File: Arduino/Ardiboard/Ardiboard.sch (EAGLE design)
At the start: 10 parts, among them IC1 ATMEGA168-20P, J1 1X5, U1 ARDUINOR3-BPLACE

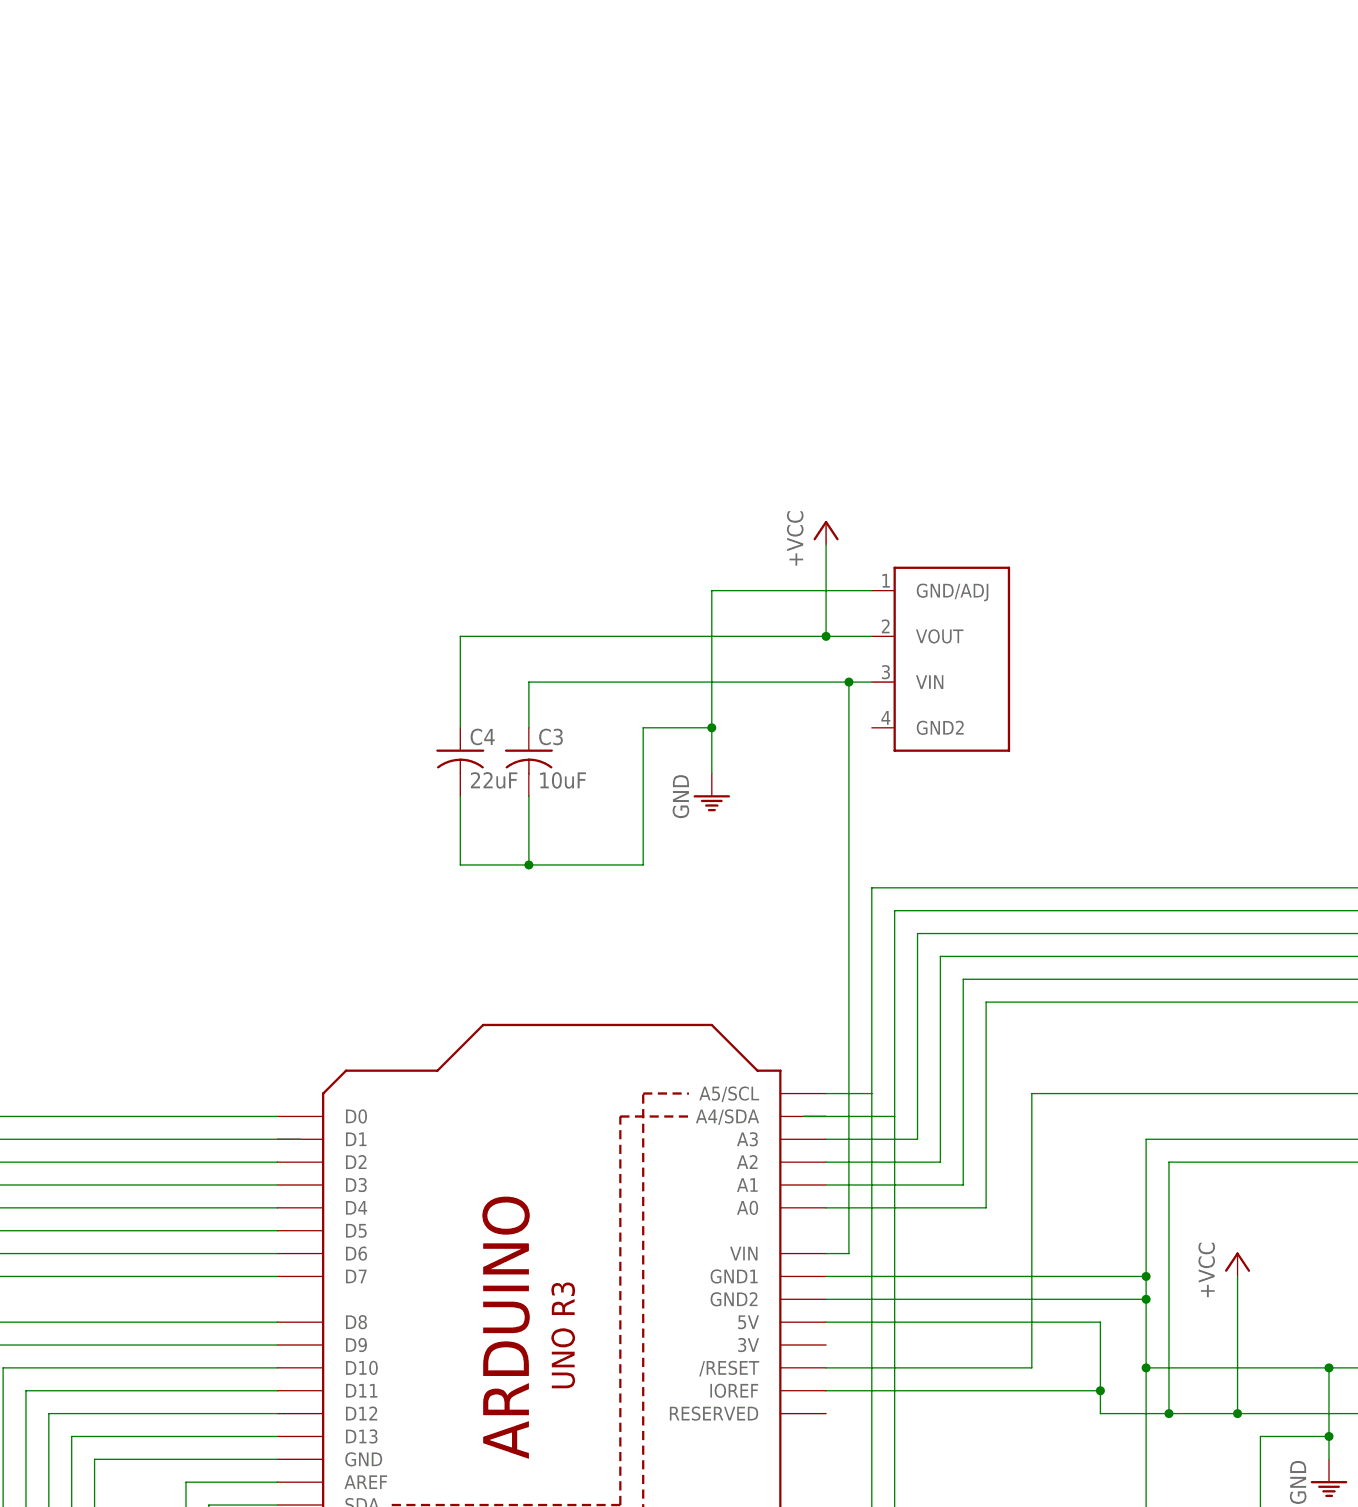
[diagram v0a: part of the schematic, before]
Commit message: added 3.3V regulator
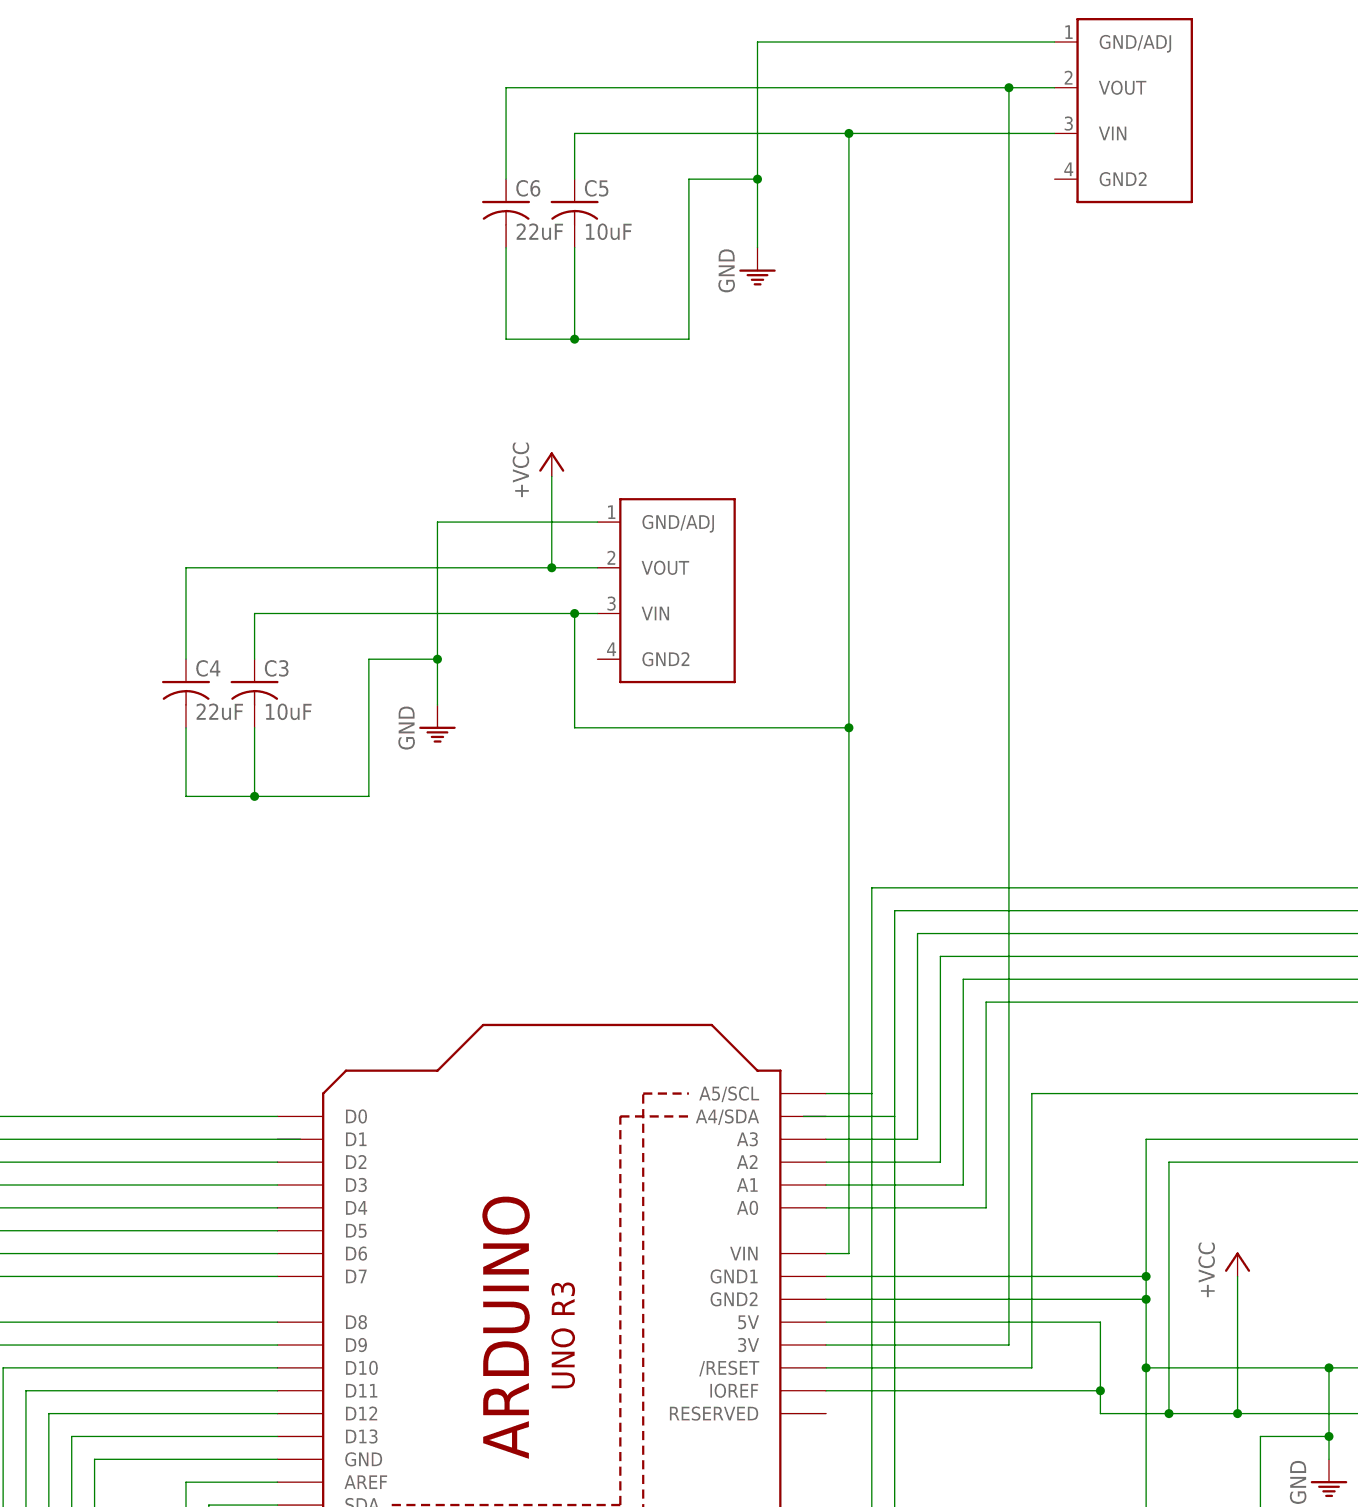
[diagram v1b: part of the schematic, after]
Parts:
- removed U$1: AZ1086-XX, voltage:AZ1086-XX
- added C5: 10uF, rcl:C-US025-030X050
- added C6: 22uF, rcl:C-US025-030X050
- added Q2: AZ1086H-5.0, voltage:AZ1086-XX
- added Q3: AZ1086H-3.3, voltage:AZ1086-XX
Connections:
- new net N$25: C3.1, C5.1, Q2.VIN, Q3.VIN, U1.VIN
- net +5V: now also Q2.VOUT; no longer U$1.VOUT
- net N$24: now also C6.1, Q3.VOUT, U1.3V; no longer C3.1, U$1.VIN, U1.VIN
- net PE: now also C5.2, C6.2, Q2.GND/ADJ, Q3.GND/ADJ; no longer U$1.GND/ADJ
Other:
- moved on the sheet: C3, C4
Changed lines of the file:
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@@
 <?xml version="1.0" encoding="utf-8"?>
 <!DOCTYPE eagle SYSTEM "eagle.dtd">
-<eagle version="6.5.0">
+<eagle version="6.6.0">
 <drawing>
 <settings>
@@
 <part name="C2" library="rcl" deviceset="C-US" device="025-025X050"/>
 <part name="P+3" library="power" deviceset="+VCC" device=""/>
-<part name="U$1" library="voltage" deviceset="AZ1086-XX" device=""/>
+<part name="Q2" library="voltage" deviceset="AZ1086-XX" device="" value="AZ1086H-5.0"/>
 <part name="GND3" library="power" deviceset="GND" device=""/>
 <part name="P+4" library="power" deviceset="+VCC" device=""/>
@@
 <part name="P+5" library="power" deviceset="+VCC" device=""/>
 <part name="GND4" library="power" deviceset="GND" device=""/>
+<part name="Q3" library="voltage" deviceset="AZ1086-XX" device="" value="AZ1086H-3.3"/>
+<part name="GND5" library="power" deviceset="GND" device=""/>
+<part name="C5" library="rcl" deviceset="C-US" device="025-030X050" value="10uF"/>
+<part name="C6" library="rcl" deviceset="C-US" device="025-030X050" value="22uF"/>
 </parts>
 <sheets>
@@
 <instance part="C2" gate="G$1" x="116.84" y="33.02"/>
 <instance part="P+3" gate="1" x="-22.86" y="33.02"/>
-<instance part="U$1" gate="G$1" x="66.04" y="132.08"/>
-<instance part="GND3" gate="M" x="40.64" y="114.3"/>
-<instance part="P+4" gate="1" x="53.34" y="144.78"/>
-<instance part="C3" gate="G$1" x="20.32" y="119.38"/>
-<instance part="C4" gate="G$1" x="12.7" y="119.38"/>
+<instance part="Q2" gate="G$1" x="35.56" y="139.7"/>
+<instance part="GND3" gate="M" x="10.16" y="121.92"/>
+<instance part="P+4" gate="1" x="22.86" y="152.4"/>
+<instance part="C3" gate="G$1" x="-10.16" y="127"/>
+<instance part="C4" gate="G$1" x="-17.78" y="127"/>
 <instance part="JP1" gate="G$1" x="248.92" y="38.1"/>
 <instance part="P+5" gate="1" x="259.08" y="60.96"/>
 <instance part="GND4" gate="M" x="259.08" y="17.78"/>
+<instance part="Q3" gate="G$1" x="86.36" y="193.04"/>
+<instance part="GND5" gate="M" x="45.72" y="172.72"/>
+<instance part="C5" gate="G$1" x="25.4" y="180.34"/>
+<instance part="C6" gate="G$1" x="17.78" y="180.34"/>
 </instances>
 <busses>
@@
 </segment>
 <segment>
-<pinref part="U$1" gate="G$1" pin="GND/ADJ"/>
-<wire x1="58.42" y1="137.16" x2="40.64" y2="137.16" width="0.1524" layer="91"/>
-<wire x1="40.64" y1="137.16" x2="40.64" y2="121.92" width="0.1524" layer="91"/>
-<wire x1="40.64" y1="121.92" x2="40.64" y2="116.84" width="0.1524" layer="91"/>
+<pinref part="Q2" gate="G$1" pin="GND/ADJ"/>
+<wire x1="27.94" y1="144.78" x2="10.16" y2="144.78" width="0.1524" layer="91"/>
+<wire x1="10.16" y1="144.78" x2="10.16" y2="129.54" width="0.1524" layer="91"/>
+<wire x1="10.16" y1="129.54" x2="10.16" y2="124.46" width="0.1524" layer="91"/>
 <pinref part="GND3" gate="M" pin="PE"/>
-<wire x1="40.64" y1="121.92" x2="33.02" y2="121.92" width="0.1524" layer="91"/>
-<wire x1="33.02" y1="121.92" x2="33.02" y2="106.68" width="0.1524" layer="91"/>
-<wire x1="33.02" y1="106.68" x2="20.32" y2="106.68" width="0.1524" layer="91"/>
-<wire x1="20.32" y1="106.68" x2="20.32" y2="114.3" width="0.1524" layer="91"/>
-<wire x1="20.32" y1="106.68" x2="12.7" y2="106.68" width="0.1524" layer="91"/>
-<wire x1="12.7" y1="106.68" x2="12.7" y2="114.3" width="0.1524" layer="91"/>
-<junction x="20.32" y="106.68"/>
-<junction x="40.64" y="121.92"/>
+<wire x1="10.16" y1="129.54" x2="2.54" y2="129.54" width="0.1524" layer="91"/>
+<wire x1="2.54" y1="129.54" x2="2.54" y2="114.3" width="0.1524" layer="91"/>
+<wire x1="2.54" y1="114.3" x2="-10.16" y2="114.3" width="0.1524" layer="91"/>
+<wire x1="-10.16" y1="114.3" x2="-10.16" y2="121.92" width="0.1524" layer="91"/>
+<wire x1="-10.16" y1="114.3" x2="-17.78" y2="114.3" width="0.1524" layer="91"/>
+<wire x1="-17.78" y1="114.3" x2="-17.78" y2="121.92" width="0.1524" layer="91"/>
+<junction x="-10.16" y="114.3"/>
+<junction x="10.16" y="129.54"/>
 <pinref part="C3" gate="G$1" pin="2"/>
 <pinref part="C4" gate="G$1" pin="2"/>
@@
 <wire x1="259.08" y1="35.56" x2="259.08" y2="20.32" width="0.1524" layer="91"/>
 <pinref part="GND4" gate="M" pin="PE"/>
+</segment>
+<segment>
+<pinref part="Q3" gate="G$1" pin="GND/ADJ"/>
+<wire x1="78.74" y1="198.12" x2="45.72" y2="198.12" width="0.1524" layer="91"/>
+<wire x1="45.72" y1="198.12" x2="45.72" y2="182.88" width="0.1524" layer="91"/>
+<wire x1="45.72" y1="182.88" x2="45.72" y2="175.26" width="0.1524" layer="91"/>
+<pinref part="GND5" gate="M" pin="PE"/>
+<wire x1="45.72" y1="182.88" x2="38.1" y2="182.88" width="0.1524" layer="91"/>
+<wire x1="38.1" y1="182.88" x2="38.1" y2="165.1" width="0.1524" layer="91"/>
+<wire x1="38.1" y1="165.1" x2="25.4" y2="165.1" width="0.1524" layer="91"/>
+<wire x1="25.4" y1="165.1" x2="25.4" y2="175.26" width="0.1524" layer="91"/>
+<wire x1="25.4" y1="165.1" x2="17.78" y2="165.1" width="0.1524" layer="91"/>
+<wire x1="17.78" y1="165.1" x2="17.78" y2="175.26" width="0.1524" layer="91"/>
+<junction x="25.4" y="165.1"/>
+<junction x="45.72" y="182.88"/>
+<pinref part="C5" gate="G$1" pin="2"/>
+<pinref part="C6" gate="G$1" pin="2"/>
 </segment>
 </net>
@@
 <segment>
 <pinref part="P+4" gate="1" pin="+5V"/>
-<wire x1="53.34" y1="142.24" x2="53.34" y2="132.08" width="0.1524" layer="91"/>
-<pinref part="U$1" gate="G$1" pin="VOUT"/>
-<wire x1="53.34" y1="132.08" x2="58.42" y2="132.08" width="0.1524" layer="91"/>
-<wire x1="53.34" y1="132.08" x2="12.7" y2="132.08" width="0.1524" layer="91"/>
-<wire x1="12.7" y1="132.08" x2="12.7" y2="121.92" width="0.1524" layer="91"/>
-<junction x="53.34" y="132.08"/>
+<wire x1="22.86" y1="149.86" x2="22.86" y2="139.7" width="0.1524" layer="91"/>
+<pinref part="Q2" gate="G$1" pin="VOUT"/>
+<wire x1="22.86" y1="139.7" x2="27.94" y2="139.7" width="0.1524" layer="91"/>
+<wire x1="22.86" y1="139.7" x2="-17.78" y2="139.7" width="0.1524" layer="91"/>
+<wire x1="-17.78" y1="139.7" x2="-17.78" y2="129.54" width="0.1524" layer="91"/>
+<junction x="22.86" y="139.7"/>
 <pinref part="C4" gate="G$1" pin="1"/>
 </segment>
@@
 </segment>
 </net>
-<net name="N$24" class="0">
+<net name="N$25" class="0">
 <segment>
 <pinref part="U1" gate="G$1" pin="VIN"/>
 <wire x1="53.34" y1="63.5" x2="55.88" y2="63.5" width="0.1524" layer="91"/>
-<wire x1="55.88" y1="63.5" x2="55.88" y2="127" width="0.1524" layer="91"/>
-<pinref part="U$1" gate="G$1" pin="VIN"/>
-<wire x1="55.88" y1="127" x2="58.42" y2="127" width="0.1524" layer="91"/>
-<wire x1="55.88" y1="127" x2="20.32" y2="127" width="0.1524" layer="91"/>
-<junction x="55.88" y="127"/>
+<wire x1="55.88" y1="63.5" x2="55.88" y2="121.92" width="0.1524" layer="91"/>
+<pinref part="Q2" gate="G$1" pin="VIN"/>
+<wire x1="27.94" y1="134.62" x2="25.4" y2="134.62" width="0.1524" layer="91"/>
 <pinref part="C3" gate="G$1" pin="1"/>
-<wire x1="20.32" y1="127" x2="20.32" y2="121.92" width="0.1524" layer="91"/>
-</segment>
-</net>
+<wire x1="25.4" y1="134.62" x2="-10.16" y2="134.62" width="0.1524" layer="91"/>
+<wire x1="-10.16" y1="134.62" x2="-10.16" y2="129.54" width="0.1524" layer="91"/>
+<wire x1="25.4" y1="134.62" x2="25.4" y2="121.92" width="0.1524" layer="91"/>
+<wire x1="25.4" y1="121.92" x2="55.88" y2="121.92" width="0.1524" layer="91"/>
+<pinref part="Q3" gate="G$1" pin="VIN"/>
+<wire x1="78.74" y1="187.96" x2="55.88" y2="187.96" width="0.1524" layer="91"/>
+<pinref part="C5" gate="G$1" pin="1"/>
+<wire x1="55.88" y1="187.96" x2="25.4" y2="187.96" width="0.1524" layer="91"/>
+<wire x1="25.4" y1="187.96" x2="25.4" y2="182.88" width="0.1524" layer="91"/>
+<wire x1="55.88" y1="121.92" x2="55.88" y2="187.96" width="0.1524" layer="91"/>
+<junction x="55.88" y="121.92"/>
+<junction x="25.4" y="134.62"/>
+<junction x="55.88" y="187.96"/>
+</segment>
+</net>
+<net name="N$24" class="0">
+<segment>
+<pinref part="Q3" gate="G$1" pin="VOUT"/>
+<wire x1="73.66" y1="193.04" x2="78.74" y2="193.04" width="0.1524" layer="91"/>
+<wire x1="73.66" y1="193.04" x2="17.78" y2="193.04" width="0.1524" layer="91"/>
+<wire x1="17.78" y1="193.04" x2="17.78" y2="182.88" width="0.1524" layer="91"/>
+<junction x="73.66" y="193.04"/>
+<pinref part="C6" gate="G$1" pin="1"/>
+<pinref part="U1" gate="G$1" pin="3V"/>
+<wire x1="53.34" y1="53.34" x2="73.66" y2="53.34" width="0.1524" layer="91"/>
+<wire x1="73.66" y1="53.34" x2="73.66" y2="193.04" width="0.1524" layer="91"/>
+</segment>
+</net>

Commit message: changed 3V regulator to pull 5V regulator
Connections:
- net +5V: now also C5.1, Q3.VIN
- net N$25: no longer C5.1, Q3.VIN
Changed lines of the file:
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@@
 <instance part="Q2" gate="G$1" x="35.56" y="139.7"/>
 <instance part="GND3" gate="M" x="10.16" y="121.92"/>
-<instance part="P+4" gate="1" x="22.86" y="152.4"/>
+<instance part="P+4" gate="1" x="22.86" y="160.02"/>
 <instance part="C3" gate="G$1" x="-10.16" y="127"/>
 <instance part="C4" gate="G$1" x="-17.78" y="127"/>
@@
 <segment>
 <pinref part="P+4" gate="1" pin="+5V"/>
-<wire x1="22.86" y1="149.86" x2="22.86" y2="139.7" width="0.1524" layer="91"/>
+<wire x1="22.86" y1="157.48" x2="22.86" y2="152.4" width="0.1524" layer="91"/>
 <pinref part="Q2" gate="G$1" pin="VOUT"/>
+<wire x1="22.86" y1="152.4" x2="22.86" y2="139.7" width="0.1524" layer="91"/>
 <wire x1="22.86" y1="139.7" x2="27.94" y2="139.7" width="0.1524" layer="91"/>
 <wire x1="22.86" y1="139.7" x2="-17.78" y2="139.7" width="0.1524" layer="91"/>
@@
 <junction x="22.86" y="139.7"/>
 <pinref part="C4" gate="G$1" pin="1"/>
+<wire x1="22.86" y1="152.4" x2="55.88" y2="152.4" width="0.1524" layer="91"/>
+<pinref part="C5" gate="G$1" pin="1"/>
+<wire x1="25.4" y1="187.96" x2="25.4" y2="182.88" width="0.1524" layer="91"/>
+<pinref part="Q3" gate="G$1" pin="VIN"/>
+<wire x1="78.74" y1="187.96" x2="55.88" y2="187.96" width="0.1524" layer="91"/>
+<wire x1="55.88" y1="187.96" x2="25.4" y2="187.96" width="0.1524" layer="91"/>
+<wire x1="55.88" y1="152.4" x2="55.88" y2="187.96" width="0.1524" layer="91"/>
+<junction x="22.86" y="152.4"/>
+<junction x="55.88" y="187.96"/>
 </segment>
 <segment>
@@
 <wire x1="25.4" y1="134.62" x2="25.4" y2="121.92" width="0.1524" layer="91"/>
 <wire x1="25.4" y1="121.92" x2="55.88" y2="121.92" width="0.1524" layer="91"/>
-<pinref part="Q3" gate="G$1" pin="VIN"/>
-<wire x1="78.74" y1="187.96" x2="55.88" y2="187.96" width="0.1524" layer="91"/>
-<pinref part="C5" gate="G$1" pin="1"/>
-<wire x1="55.88" y1="187.96" x2="25.4" y2="187.96" width="0.1524" layer="91"/>
-<wire x1="25.4" y1="187.96" x2="25.4" y2="182.88" width="0.1524" layer="91"/>
-<wire x1="55.88" y1="121.92" x2="55.88" y2="187.96" width="0.1524" layer="91"/>
-<junction x="55.88" y="121.92"/>
 <junction x="25.4" y="134.62"/>
-<junction x="55.88" y="187.96"/>
-</segment>
-</net>
+</segment>
+</net>
